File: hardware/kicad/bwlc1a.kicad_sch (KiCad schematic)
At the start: 0 parts

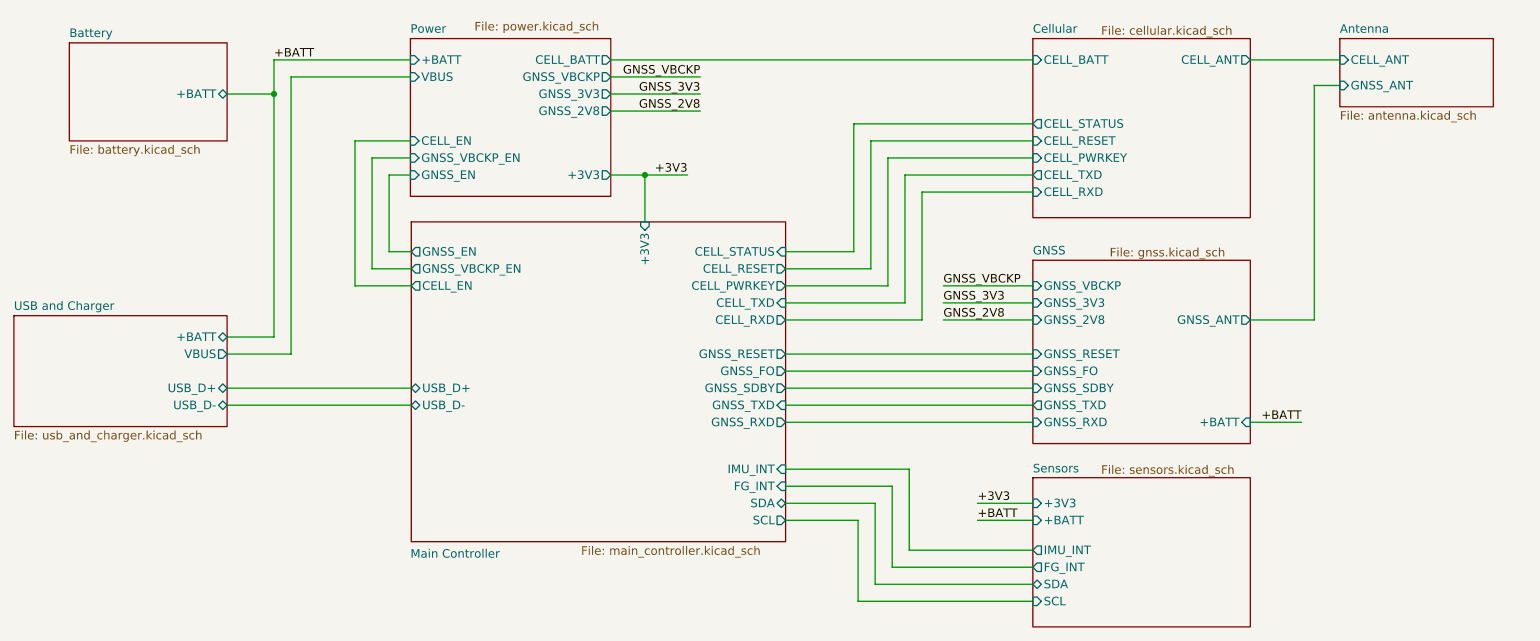
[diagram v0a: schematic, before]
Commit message: GNSS and Antenna Update
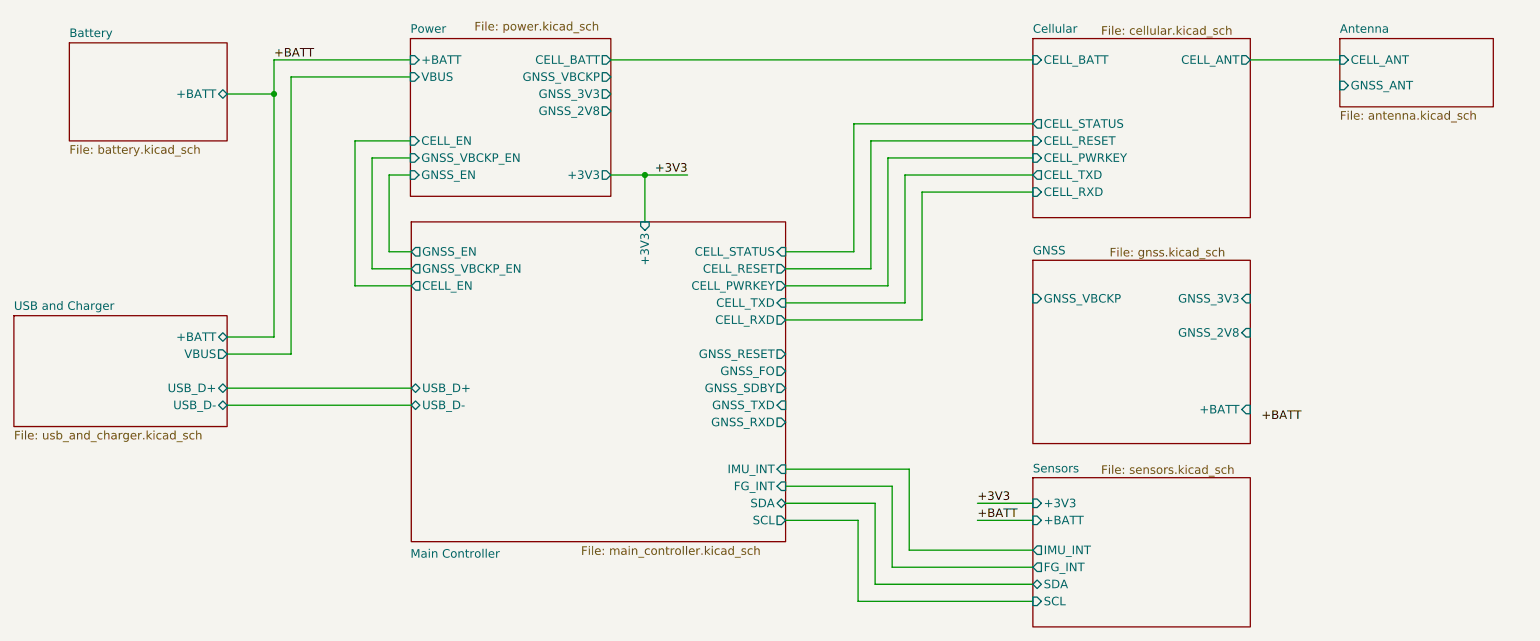
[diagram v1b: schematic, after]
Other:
- sheet GNSS ports: added none; removed GNSS_ANT, GNSS_FO, GNSS_RESET, GNSS_RXD, GNSS_SDBY, GNSS_TXD

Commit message: Update Sch for GNSS and main controller
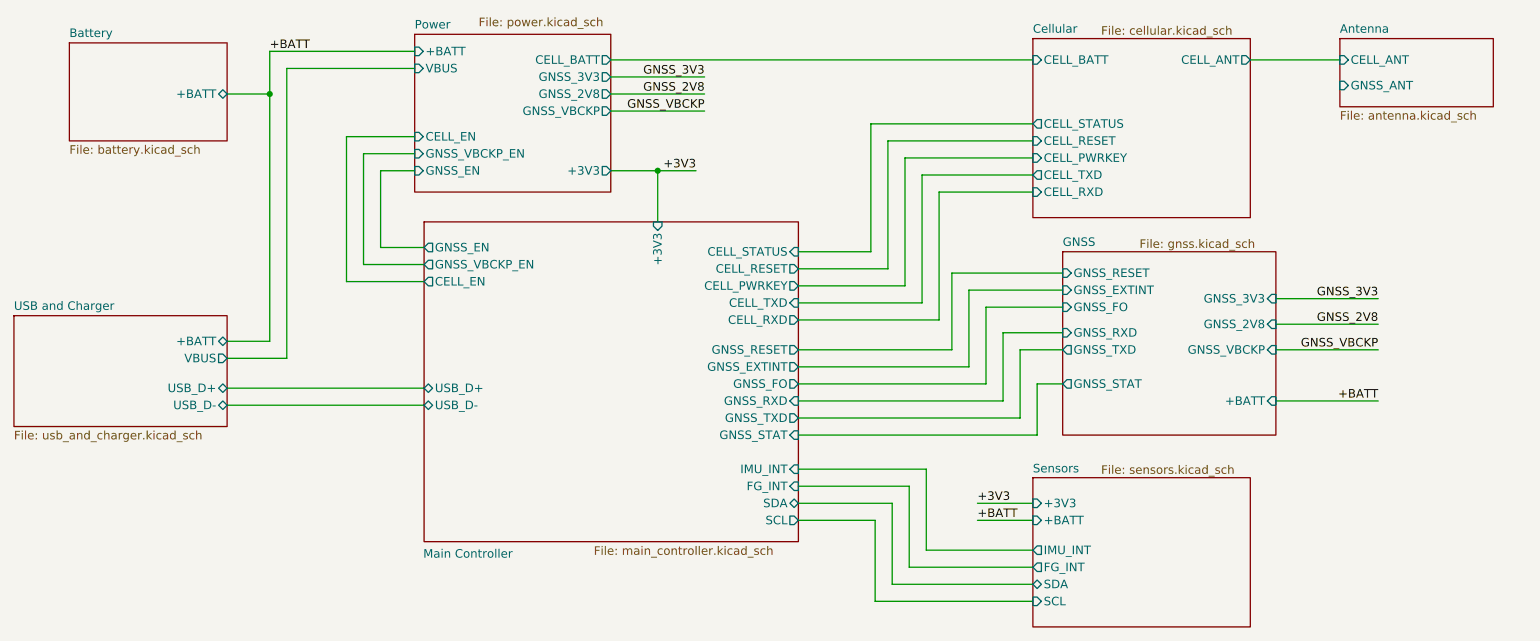
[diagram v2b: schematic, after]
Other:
- sheet GNSS ports: added GNSS_EXTINT, GNSS_FO, GNSS_RESET, GNSS_RXD, GNSS_STAT, GNSS_TXD; removed none
- sheet Main Controller ports: added GNSS_EXTINT, GNSS_STAT; removed GNSS_SDBY

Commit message: Update for PCB Layout
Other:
- sheet GNSS ports: added GNSS_GEOFENCE, GNSS_JAMDET; removed GNSS_2V8
- sheet Main Controller ports: added GNSS_GEOFENCE, GNSS_JAMDET; removed none

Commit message: Finish Manufacturing File
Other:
- sheet Antenna ports: added none; removed GNSS_ANT
- sheet Main Controller ports: added none; removed GNSS_GEOFENCE, GNSS_JAMDET
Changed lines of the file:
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@@
 	(wire
 		(pts
-			(xy 185.42 90.17) (xy 193.04 90.17)
-		)
-		(stroke
-			(width 0)
-			(type default)
-		)
-	)
-	(wire
-		(pts
-			(xy 186.69 101.6) (xy 186.69 92.71)
+			(xy 182.88 90.17) (xy 193.04 90.17)
+		)
+		(stroke
+			(width 0)
+			(type default)
+		)
+	)
+	(wire
+		(pts
+			(xy 185.42 104.14) (xy 185.42 92.71)
 		)
 		(stroke
@@
 	(wire
 		(pts
-			(xy 153.67 93.98) (xy 182.88 93.98)
+			(xy 153.67 96.52) (xy 177.8 96.52)
 		)
 		(stroke
@@
 	(wire
 		(pts
+			(xy 193.04 100.33) (xy 190.5 100.33)
+		)
+		(stroke
+			(width 0)
+			(type default)
+		)
+	)
+	(wire
+		(pts
+			(xy 190.5 109.22) (xy 153.67 109.22)
+		)
+		(stroke
+			(width 0)
+			(type default)
+		)
+	)
+	(wire
+		(pts
 			(xy 68.58 104.775) (xy 97.917 104.775)
 		)
@@
 	(wire
 		(pts
-			(xy 153.67 101.6) (xy 186.69 101.6)
+			(xy 153.67 104.14) (xy 185.42 104.14)
 		)
 		(stroke
@@
 	(wire
 		(pts
-			(xy 182.88 85.09) (xy 193.04 85.09)
+			(xy 177.8 85.09) (xy 193.04 85.09)
 		)
 		(stroke
@@
 	(wire
 		(pts
-			(xy 187.96 104.14) (xy 187.96 95.25)
-		)
-		(stroke
-			(width 0)
-			(type default)
-		)
-	)
-	(wire
-		(pts
-			(xy 186.69 92.71) (xy 193.04 92.71)
+			(xy 187.96 106.68) (xy 187.96 95.25)
+		)
+		(stroke
+			(width 0)
+			(type default)
+		)
+	)
+	(wire
+		(pts
+			(xy 185.42 92.71) (xy 193.04 92.71)
 		)
 		(stroke
@@
 	(wire
 		(pts
-			(xy 153.67 99.06) (xy 185.42 99.06)
+			(xy 153.67 101.6) (xy 182.88 101.6)
 		)
 		(stroke
@@
 	(wire
 		(pts
-			(xy 182.88 93.98) (xy 182.88 85.09)
+			(xy 177.8 96.52) (xy 177.8 85.09)
 		)
 		(stroke
@@
 	(wire
 		(pts
-			(xy 184.15 96.52) (xy 184.15 87.63)
+			(xy 180.34 99.06) (xy 180.34 87.63)
 		)
 		(stroke
@@
 	(wire
 		(pts
-			(xy 153.67 104.14) (xy 187.96 104.14)
+			(xy 153.67 106.68) (xy 187.96 106.68)
 		)
 		(stroke
@@
 	(wire
 		(pts
+			(xy 190.5 100.33) (xy 190.5 109.22)
+		)
+		(stroke
+			(width 0)
+			(type default)
+		)
+	)
+	(wire
+		(pts
 			(xy 132.715 69.85) (xy 132.715 77.47)
 		)
@@
 	(wire
 		(pts
-			(xy 153.67 96.52) (xy 184.15 96.52)
+			(xy 153.67 99.06) (xy 180.34 99.06)
 		)
 		(stroke
@@
 	(wire
 		(pts
-			(xy 185.42 99.06) (xy 185.42 90.17)
-		)
-		(stroke
-			(width 0)
-			(type default)
-		)
-	)
-	(wire
-		(pts
-			(xy 184.15 87.63) (xy 193.04 87.63)
+			(xy 182.88 101.6) (xy 182.88 90.17)
+		)
+		(stroke
+			(width 0)
+			(type default)
+		)
+	)
+	(wire
+		(pts
+			(xy 180.34 87.63) (xy 193.04 87.63)
 		)
 		(stroke
@@
 		)
 		(pin "GNSS_RESET" output
-			(at 153.67 93.98 0)
+			(at 153.67 96.52 0)
 			(effects
 				(font
@@
 		)
 		(pin "GNSS_RXD" input
+			(at 153.67 104.14 0)
+			(effects
+				(font
+					(size 1.27 1.27)
+				)
+				(justify right)
+			)
+		)
+		(pin "GNSS_TXD" output
+			(at 153.67 106.68 0)
+			(effects
+				(font
+					(size 1.27 1.27)
+				)
+				(justify right)
+			)
+		)
+		(pin "GNSS_FO" output
 			(at 153.67 101.6 0)
 			(effects
@@
 			)
 		)
-		(pin "GNSS_TXD" output
-			(at 153.67 104.14 0)
-			(effects
-				(font
-					(size 1.27 1.27)
-				)
-				(justify right)
-			)
-		)
-		(pin "GNSS_FO" output
+		(pin "GNSS_EXTINT" output
 			(at 153.67 99.06 0)
 			(effects
@@
 			)
 		)
-		(pin "GNSS_EXTINT" output
-			(at 153.67 96.52 0)
-			(effects
-				(font
-					(size 1.27 1.27)
-				)
-				(justify right)
-			)
-		)
 		(pin "GNSS_STAT" input
-			(at 153.67 106.68 0)
-			(effects
-				(font
-					(size 1.27 1.27)
-				)
-				(justify right)
-			)
-		)
-		(pin "GNSS_JAMDET" input
 			(at 153.67 109.22 0)
-			(effects
-				(font
-					(size 1.27 1.27)
-				)
-				(justify right)
-			)
-		)
-		(pin "GNSS_GEOFENCE" input
-			(at 153.67 111.76 0)
 			(effects
 				(font
@@
 	(sheet
 		(at 234.315 50.165)
-		(size 22.86 10.16)
+		(size 22.86 5.715)
 		(fields_autoplaced yes)
 		(stroke
@@
 		)
 		(property "Sheetfile" "antenna.kicad_sch"
-			(at 234.315 60.9096 0)
+			(at 234.315 56.4646 0)
 			(effects
 				(font
@@
 			(effects
 				(font
-					(size 1.27 1.27)
-				)
-				(justify left)
-			)
-		)
-		(pin "GNSS_ANT" input
-			(at 234.315 57.15 180)
-			(effects
-				(font

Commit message: update
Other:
- sheet GNSS ports: added none; removed GNSS_GEOFENCE, GNSS_JAMDET
- sheet Power ports: added none; removed GNSS_2V8
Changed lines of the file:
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@@
-	(wire
-		(pts
-			(xy 125.73 58.42) (xy 139.7 58.42)
-		)
-		(stroke
-			(width 0)
-			(type default)
-		)
-	)
 	(wire
 		(pts
@@
 		)
 	)
-	(label "GNSS_2V8"
-		(at 139.7 58.42 180)
-		(fields_autoplaced yes)
-		(effects
-			(font
-				(size 1.27 1.27)
-			)
-			(justify right bottom)
-		)
-	)
 	(label "+3V3"
 		(at 180.34 119.38 0)
@@
 			)
 		)
-		(pin "GNSS_JAMDET" output
-			(at 193.04 102.87 180)
-			(effects
-				(font
-					(size 1.27 1.27)
-				)
-				(justify left)
-			)
-		)
-		(pin "GNSS_GEOFENCE" output
-			(at 193.04 105.41 180)
-			(effects
-				(font
-					(size 1.27 1.27)
-				)
-				(justify left)
-			)
-		)
 		(instances
 			(project "bwlc1a"
@@
 			(effects
 				(font
-					(size 1.27 1.27)
-				)
-				(justify right)
-			)
-		)
-		(pin "GNSS_2V8" output
-			(at 125.73 58.42 0)
-			(effects
-				(font
